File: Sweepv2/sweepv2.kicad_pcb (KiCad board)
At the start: 2 copper layers, 217.3 x 86.9 mm, 51 parts, among them J1 AudioJack4dpb, J2 AudioJack4dpb, SW10 SW_Push, SW11 SW_Push, SW11_r1 SW_Push, SW12 SW_Push, SW12_r1 SW_Push, SW13_r1 SW_Push, SW14 SW_Push, SW15 SW_Push, SW15_r1 SW_Push, SW16 SW_Push, SW16_r1 SW_Push, SW17 SW_Push, SW17_r1 SW_Push, SW18 SW_Push, SW18_r1 SW_Push, SW2 SW_Push, SW20 SW_Push, SW20_r1 SW_Push, SW21 SW_Push, SW21_r1 SW_Push, SW2_r1 SW_Push, SW3 SW_Push, SW3_r1 SW_Push, SW4 SW_Push, SW4_r1 SW_Push, SW5 SW_Push, SW5_r1 SW_Push, SW6 SW_Push, SW6_r1 SW_Push, SW7_r1 SW_Push, SW8 SW_Push, SW8_r1 SW_Push, SW9 SW_Push, SW9_r1 SW_Push, U1 ProMicro-kbd, U2 ProMicro-kbd

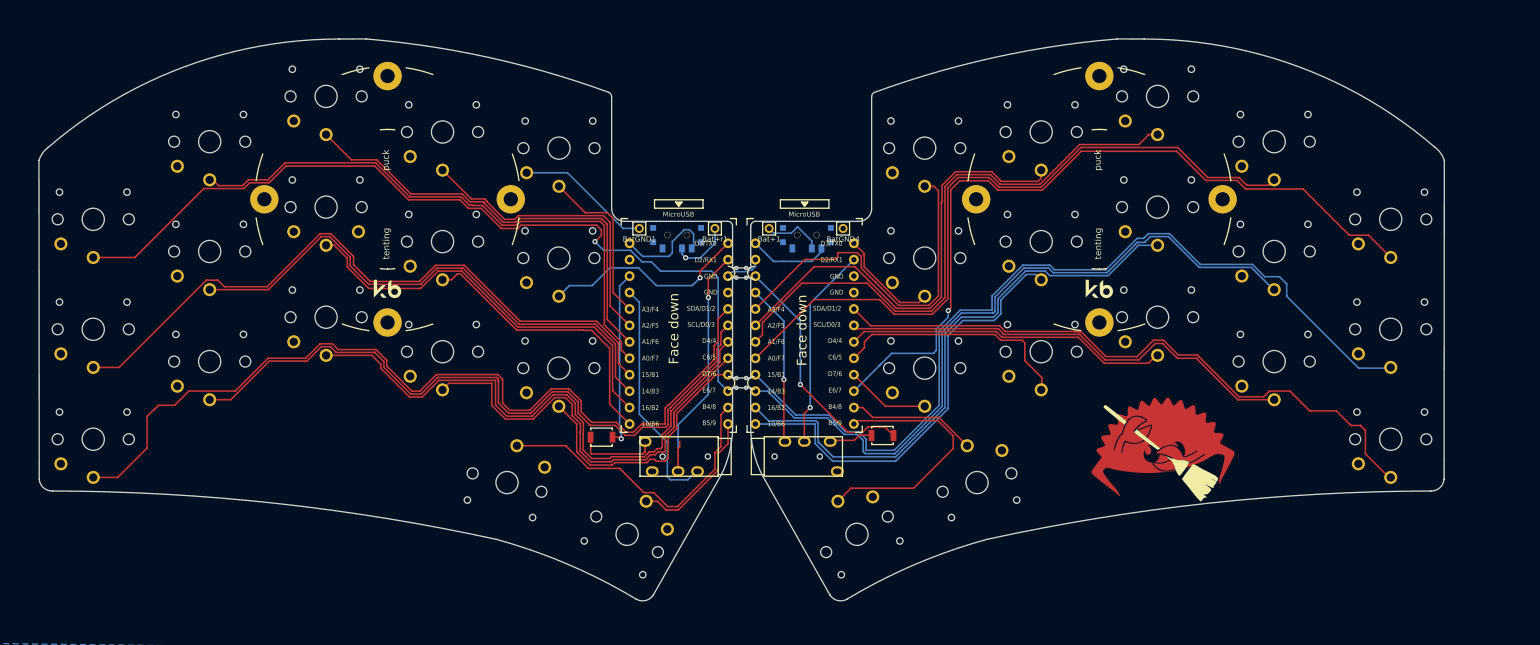
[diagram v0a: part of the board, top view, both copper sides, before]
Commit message: address issues raised...
'fix' the silk issue. change the way the boards are joined, move the controllers slightly away from edge, slight re route. add a bit of text about the ferris?
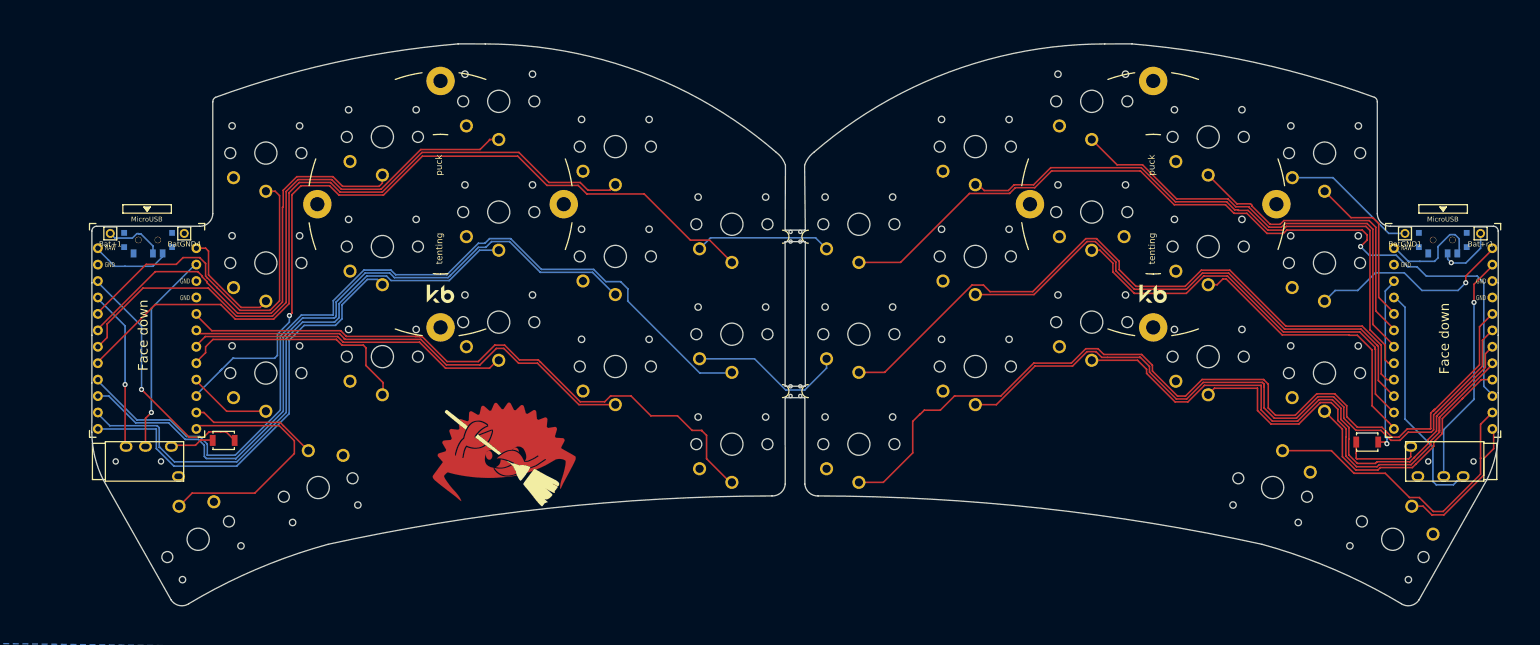
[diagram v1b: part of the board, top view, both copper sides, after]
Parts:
- U1, U2: footprint kbd:ProMicro_v3 -> kbd:ProMicro_v3_min
- moved J2 118.4 mm to (237.0, 78.4)
- moved REF** 118.4 mm to (185.9, 38.7)
- moved RSW1 118.4 mm to (218.9, 75.4)
- moved SW10 118.4 mm to (176.4, 39.9)
- moved SW11 118.4 mm to (194.4, 45.2)
- moved SW14 118.4 mm to (140.4, 75.8)
- moved SW15 118.4 mm to (158.4, 63.8)
- moved SW16 118.4 mm to (176.4, 56.9)
- moved SW17 118.4 mm to (194.4, 62.2)
- moved SW2 118.4 mm to (140.4, 41.8)
- moved SW20 118.4 mm to (222.9, 90.5)
- moved SW21 118.4 mm to (204.3, 82.5)
- moved SW3 118.4 mm to (158.4, 29.8)
- moved SW4 118.4 mm to (176.4, 22.8)
- moved SW5 118.4 mm to (194.4, 28.3)
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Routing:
- net gnd: track 47.1 -> 86.3 mm
- net Switch18: track 40.4 -> 35.7 mm
- net Switch15: track 41.8 -> 40.1 mm
- net Switch14: track 69.6 -> 68.6 mm
- net Switch10_r: track 16.4 -> 17.2 mm
- net Switch13: track 91.2 -> 90.5 mm
- net Switch6: track 106.0 -> 106.6 mm
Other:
- board size 217.3 x 86.9 mm -> 217.4 x 86.9 mm
- board text added: "Sweep is based on the Ferris."
- board text added: "Sweep v 2.1"
